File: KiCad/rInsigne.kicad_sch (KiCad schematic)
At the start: 46 parts, among them CN1 PH2.0-2P-LT, J1 Connector, USB-TYPE-C-16P, Q1 MMBT2222A 1P, SW2 MINI MSK12CO2, U2 MCP73871-2CA, U3 AP2112K-3.3TRG1, U4 ESP32-S3-MINI-1-N8

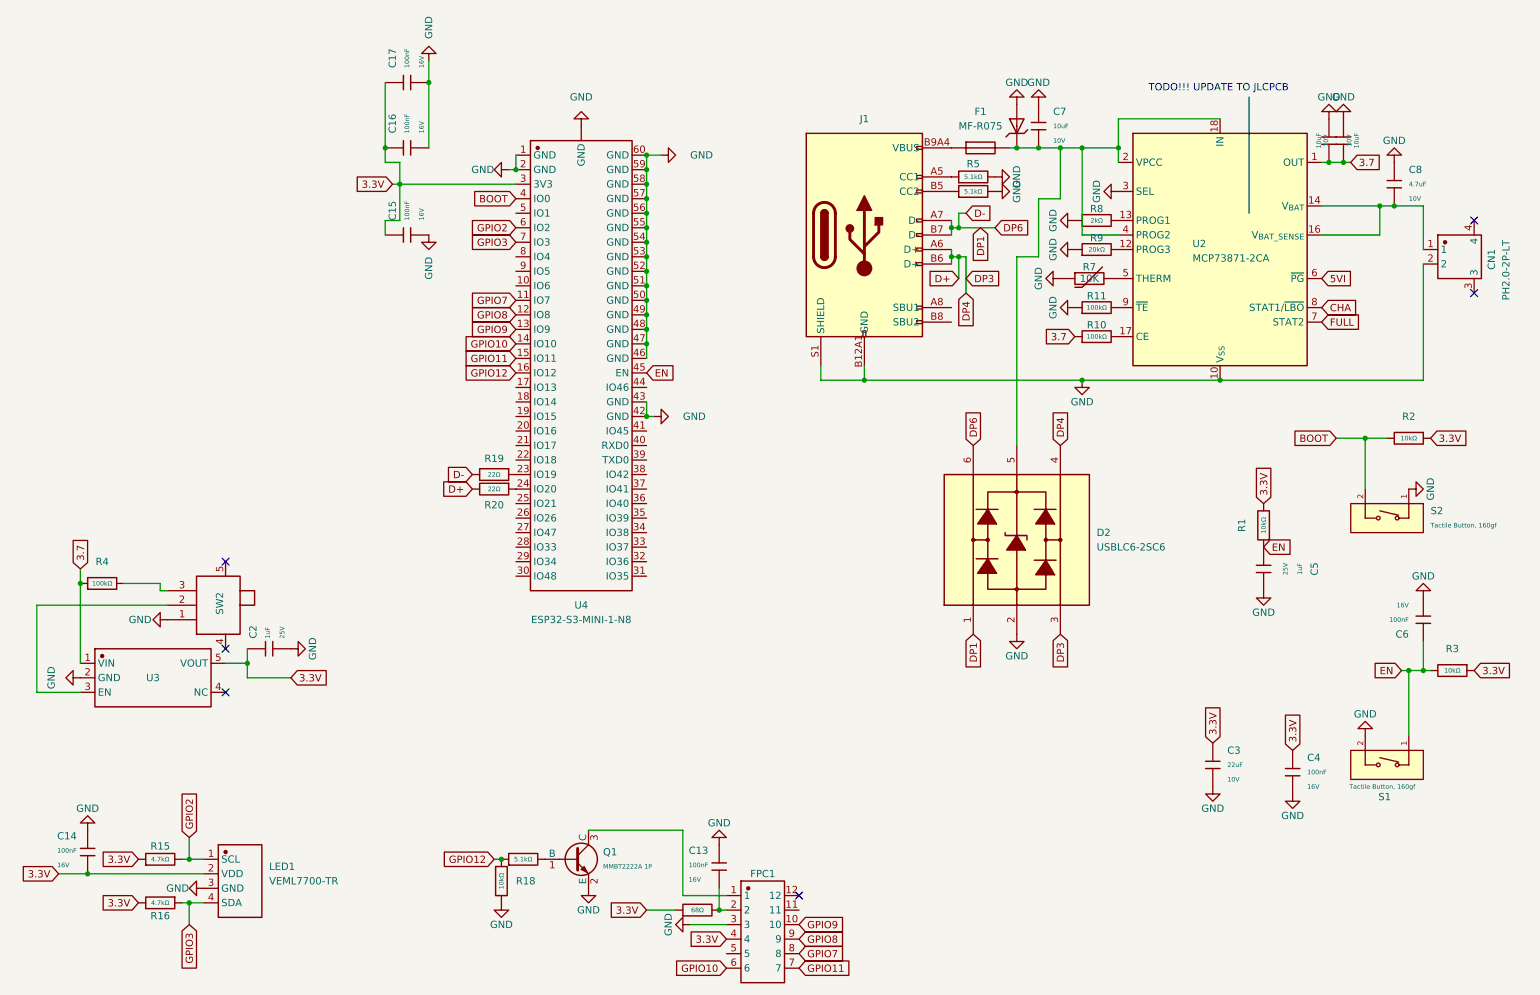
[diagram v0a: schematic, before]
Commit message: Updated the Battery driver to its JLCPCB version
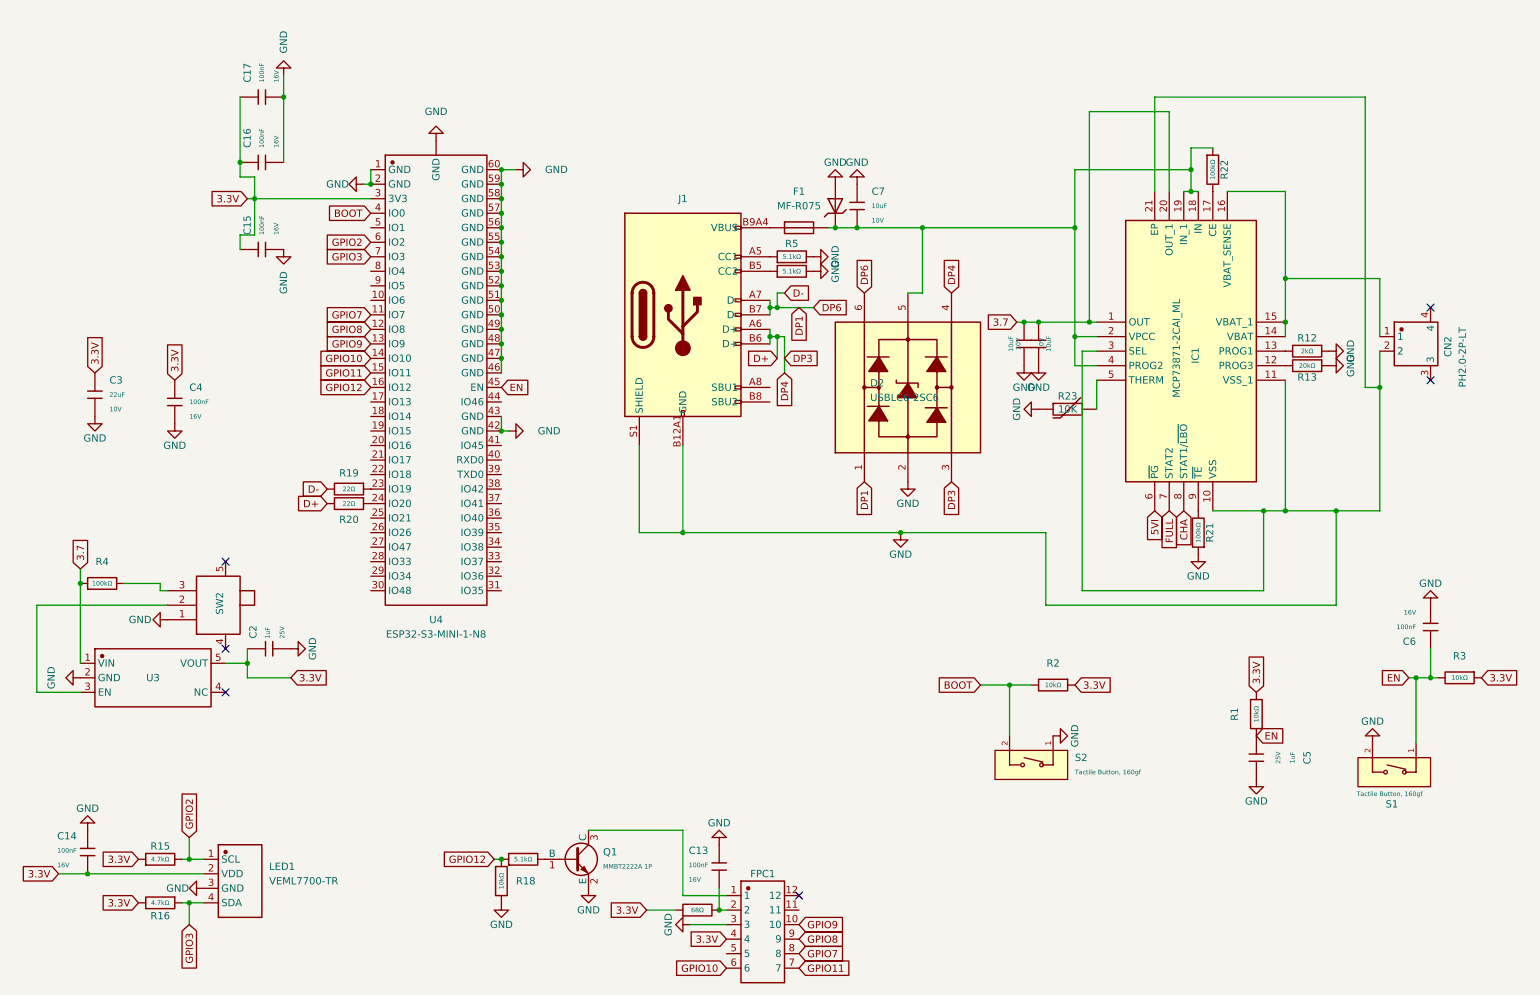
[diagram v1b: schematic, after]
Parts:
- removed C8: 4.7uF, PCM_JLCPCB:C_0402, symbol PCM_JLCPCB-Capacitors:0402,4.7uF
- removed CN1: PH2.0-2P-LT, JLPCB_ext:CONN-SMD_PH2.0-1X2PW, symbol JLPCB_ext:PH2.0-2P-LT
- removed R10, R11: 100kΩ, PCM_JLCPCB:R_0402, symbol PCM_JLCPCB-Resistors:0402,100kΩ
- removed R7: 10K, JLPCB_ext:NCP15XH103F03RC, symbol JLPCB_ext:NCP15XH103F03RC
- removed R8: 2kΩ, PCM_JLCPCB:R_0402, symbol PCM_JLCPCB-Resistors:0402,2kΩ
- removed R9: 20kΩ, PCM_JLCPCB:R_0402, symbol PCM_JLCPCB-Resistors:0402,20kΩ
- removed U2: MCP73871-2CA, Package_DFN_QFN:QFN-20-1EP_4x4mm_P0.5mm_EP2.5x2.5mm, symbol Battery_Management:MCP73871-2CA
- added CN2: PH2.0-2P-LT, JLPCB_ext:CONN-SMD_PH2.0-1X2PW, symbol JLPCB_ext:PH2.0-2P-LT
- added IC1: MCP73871-2CAI_ML, QFN50P400X400X100-21N-D, symbol JLPCB_ext:MCP73871-2CAI_ML
- added R12: 2kΩ, PCM_JLCPCB:R_0402, symbol PCM_JLCPCB-Resistors:0402,2kΩ
- added R13: 20kΩ, PCM_JLCPCB:R_0402, symbol PCM_JLCPCB-Resistors:0402,20kΩ
- added R21, R22: 100kΩ, PCM_JLCPCB:R_0402, symbol PCM_JLCPCB-Resistors:0402,100kΩ
- added R23: 10K, JLPCB_ext:NCP15XH103F03RC, symbol JLPCB_ext:NCP15XH103F03RC
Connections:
- net 3.7: now also IC1.1 (OUT), IC1.20 (OUT_1)
- net 5VI: now also IC1.6 (~{PG})
- net CHA: now also IC1.8 (STAT1/~{LBO})
- net FULL: now also IC1.7 (STAT2)
- net GND: now also CN2.2, IC1.10 (VSS), IC1.11 (VSS_1), IC1.21 (EP), IC1.3 (SEL), R12.1, R13.1, R21.1, R23.1
- net at C7.1, D1.1, D2.5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: now also IC1.18 (IN), IC1.19 (IN_1), IC1.2 (VPCC), IC1.4 (PROG2), R22.1
- new net: IC1.17 (CE), R22.2
- new net: IC1.12 (PROG3), R13.2
- new net: IC1.13 (PROG1), R12.2
- new net: CN2.1, IC1.14 (VBAT), IC1.15 (VBAT_1), IC1.16 (VBAT_SENSE)
- new net: IC1.5 (THERM), R23.2
- new net: IC1.9 (~{TE}), R21.2
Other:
- note removed: "TODO!!! UPDATE TO JLCPCB"
- moved on the sheet: C15, C16, C17, C3, C4, C5, C6, C7, D2, F1, J1, R1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
